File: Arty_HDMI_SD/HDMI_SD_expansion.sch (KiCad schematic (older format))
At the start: 54 parts, among them J2 1140084168, J4 2000-1-2-41-00-BK, J5 UE27AC54100, U1 TPS61232DRCT, U2 MAX3421EEHJ, Y1 KX-7_12,MHz

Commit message: Bug Fix
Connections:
- wire segments 238 -> 241
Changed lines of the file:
@@
+	1    0    0    -1
+$EndComp
+Wire Wire Line
+	6125 3600 6125 4125
+Wire Wire Line
+	5750 3600 5750 3750
+Wire Wire Line
+	6125 3600 5750 3600
+$Comp
+L power:GND #PWR?
+U 1 1 5D90A22E
+P 5750 3750
+F 0 "#PWR?" H 5750 3500 50  0001 C CNN
+F 1 "GND" H 5755 3577 50  0000 C CNN
+F 2 "" H 5750 3750 50  0001 C CNN
+F 3 "" H 5750 3750 50  0001 C CNN
+	1    5750 3750
 	1    0    0    -1
 $EndComp

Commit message: Added more testpads
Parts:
- added TP11, TP12, TP13, TP14, TP15: TP_SMD1MM, antmicro-footprints:Testpoint_smd_1mm, symbol antmicro_Test_Points:TP_SMD1MM
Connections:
- wire segments 241 -> 246
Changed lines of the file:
@@
 	6125 3600 5750 3600
 $Comp
-L power:GND #PWR?
+L power:GND #PWR01
 U 1 1 5D90A22E
 P 5750 3750
-F 0 "#PWR?" H 5750 3500 50  0001 C CNN
+F 0 "#PWR01" H 5750 3500 50  0001 C CNN
 F 1 "GND" H 5755 3577 50  0000 C CNN
 F 2 "" H 5750 3750 50  0001 C CNN
@@
 	1    0    0    -1
 $EndComp
+Wire Wire Line
+	9050 2100 8500 2100
+Wire Wire Line
+	9050 2200 8500 2200
+Wire Wire Line
+	9850 2300 10450 2300
+Wire Wire Line
+	9850 2400 10450 2400
+Wire Wire Line
+	9050 2400 8500 2400
+$Comp
+L antmicro_Test_Points:TP_SMD1MM TP11
+U 1 1 5D86FB45
+P 8400 2100
+F 0 "TP11" V 8400 2000 50  0000 C CNN
+F 1 "TP_SMD1MM" H 8400 2000 50  0001 C CNN
+F 2 "antmicro-footprints:Testpoint_smd_1mm" H 8600 2300 60  0001 L CNN
+F 3 "" H 8600 2400 60  0001 L CNN
+	1    8400 2100
+	0    1    1    0
+$EndComp
+$Comp
+L antmicro_Test_Points:TP_SMD1MM TP12
+U 1 1 5D86FCBB
+P 8400 2200
+F 0 "TP12" V 8400 2100 50  0000 C CNN
+F 1 "TP_SMD1MM" H 8400 2100 50  0001 C CNN
+F 2 "antmicro-footprints:Testpoint_smd_1mm" H 8600 2400 60  0001 L CNN
+F 3 "" H 8600 2500 60  0001 L CNN
+	1    8400 2200
+	0    1    1    0
+$EndComp
+$Comp
+L antmicro_Test_Points:TP_SMD1MM TP13
+U 1 1 5D86FD3B
+P 8400 2400
+F 0 "TP13" V 8400 2300 50  0000 C CNN
+F 1 "TP_SMD1MM" H 8400 2300 50  0001 C CNN
+F 2 "antmicro-footprints:Testpoint_smd_1mm" H 8600 2600 60  0001 L CNN
+F 3 "" H 8600 2700 60  0001 L CNN
+	1    8400 2400
+	0    1    1    0
+$EndComp
+$Comp
+L antmicro_Test_Points:TP_SMD1MM TP15
+U 1 1 5D86FDC5
+P 10550 2400
+F 0 "TP15" V 10550 2300 50  0000 C CNN
+F 1 "TP_SMD1MM" H 10550 2300 50  0001 C CNN
+F 2 "antmicro-footprints:Testpoint_smd_1mm" H 10750 2600 60  0001 L CNN
+F 3 "" H 10750 2700 60  0001 L CNN
+	1    10550 2400
+	0    -1   -1   0
+$EndComp
+$Comp
+L antmicro_Test_Points:TP_SMD1MM TP14
+U 1 1 5D86FF1F
+P 10550 2300
+F 0 "TP14" V 10550 2200 50  0000 C CNN
+F 1 "TP_SMD1MM" H 10550 2200 50  0001 C CNN
+F 2 "antmicro-footprints:Testpoint_smd_1mm" H 10750 2500 60  0001 L CNN
+F 3 "" H 10750 2600 60  0001 L CNN
+	1    10550 2300
+	0    -1   -1   0
+$EndComp
 $EndSCHEMATC

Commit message: Added TVS
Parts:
- removed C2, C3, C4, C5, C6, C7, C8, C9: C_100n_0402_6V3, antmicro-footprints:0402-cap, symbol HDMI_SD_expansion-rescue:C_100n_0402_6V3-antmicro_Capacitors_0402
- added IC1: TPD8S009DSMR, antmicro-footprints:R-PDSO-N15, symbol antmicroTVSDiodes:TPD8S009DSMR
- added R13, R14, R15, R16, R17, R18, R19, R20: R_0R_0402, antmicro-footprints:0402-res, symbol antmicroResistors0402:R_0R_0402
- C10, C12, C13, C14: symbol antmicro_Capacitors_0603:C_22u_0603 -> HDMI_SD_expansion-rescue:C_22u_0603-antmicro_Capacitors_0603
- C11: symbol antmicro_Capacitors_0402:C_10n_0402 -> HDMI_SD_expansion-rescue:C_10n_0402-antmicro_Capacitors_0402
- C16, C17: symbol antmicro_Capacitors_0402:C_22p_0402 -> HDMI_SD_expansion-rescue:C_22p_0402-antmicro_Capacitors_0402
- D1, D2: symbol antmicro_TVS_Diodes:PGB1010603MR -> HDMI_SD_expansion-rescue:PGB1010603MR-antmicro_TVS_Diodes
- J2: symbol antmicro_Memory_Connectors_PC_Card_Sockets:1140084168 -> HDMI_SD_expansion-rescue:1140084168-antmicro_Memory_Connectors_PC_Card_Sockets
- J4: symbol antmicro_USB_DVI_HDMI_Connectors:2000-1-2-41-00-BK -> HDMI_SD_expansion-rescue:2000-1-2-41-00-BK-antmicro_USB_DVI_HDMI_Connectors
- J5: symbol antmicro_USB_DVI_HDMI_Connectors:UE27AC54100 -> HDMI_SD_expansion-rescue:UE27AC54100-antmicro_USB_DVI_HDMI_Connectors
- JB1, JC1, JD1: symbol antmicro_Rectangular_Connectors_Headers_Male_Pins:0015912120 -> HDMI_SD_expansion-rescue:0015912120-antmicro_Rectangular_Connectors_Headers_Male_Pins
- L1: symbol antmicro_Fixed_Inductors:XFL4020-102MEB -> HDMI_SD_expansion-rescue:XFL4020-102MEB-antmicro_Fixed_Inductors
- N1: symbol antmicro_Mechanical_Parts:antmicro_logo -> HDMI_SD_expansion-rescue:antmicro_logo-antmicro_Mechanical_Parts
- R1, R2, R3, R4, R5, R6, R7: symbol antmicro_Resistors_0603:R_20k_0603 -> HDMI_SD_expansion-rescue:R_20k_0603-antmicro_Resistors_0603
- R10, R9: symbol antmicro_Resistors_0402:R_22R_0402 -> HDMI_SD_expansion-rescue:R_22R_0402-antmicro_Resistors_0402
- R11: symbol antmicro_Resistors_0603:R_10k_0603 -> HDMI_SD_expansion-rescue:R_10k_0603-antmicro_Resistors_0603
- R12: symbol antmicro_Resistors_0402:R_220R_0402 -> HDMI_SD_expansion-rescue:R_220R_0402-antmicro_Resistors_0402
- R8: symbol antmicro_Resistors_0603:R_0R_0603 -> HDMI_SD_expansion-rescue:R_0R_0603-antmicro_Resistors_0603
- TP1, TP10, TP11, TP12, TP13, TP14, TP15, TP2, TP3, TP4, TP5, TP6, TP7, TP8, TP9: symbol antmicro_Test_Points:TP_SMD1MM -> HDMI_SD_expansion-rescue:TP_SMD1MM-antmicro_Test_Points
- U1: symbol antmicro_DC_DC_Converters:TPS61232DRCT -> HDMI_SD_expansion-rescue:TPS61232DRCT-antmicro_DC_DC_Converters
- U2: symbol antmicro_Interface_Controllers:MAX3421EEHJ -> HDMI_SD_expansion-rescue:MAX3421EEHJ-antmicro_Interface_Controllers
- Y1: symbol antmicro_Oscillators:KX-7_12,MHz -> HDMI_SD_expansion-rescue:KX-7_12,MHz-antmicro_Oscillators
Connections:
- wire segments 246 -> 270
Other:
- note removed: "caps will be replaced with 0R by default"

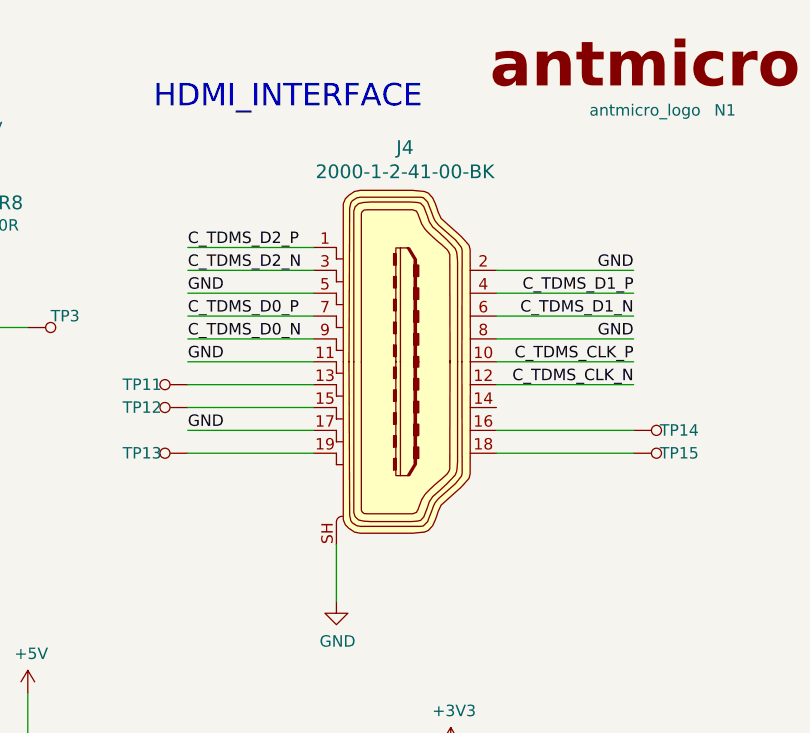
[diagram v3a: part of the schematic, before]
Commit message: Changed HDMI connector through hole
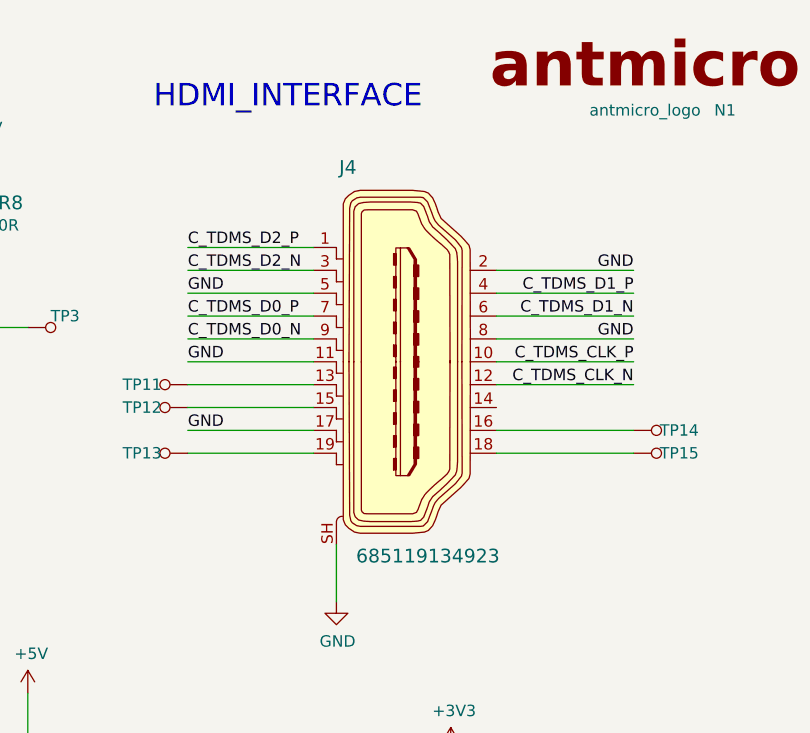
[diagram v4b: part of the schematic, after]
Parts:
- removed J4: 2000-1-2-41-00-BK, antmicro-footprints:HDMI_A_Female_2000-1-2-41-00-BK, symbol HDMI_SD_expansion-rescue:2000-1-2-41-00-BK-antmicro_USB_DVI_HDMI_Connectors
- added J4: 685119134923, antmicro-footprints:HDMI_A_Female_685119134923, symbol antmicroUSBDVIHDMIConnectors:685119134923
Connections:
- net C_TDMS_CLK_N: now also J4.12
- net C_TDMS_CLK_P: now also J4.10
- net C_TDMS_D0_N: now also J4.9
- net C_TDMS_D0_P: now also J4.7
- net C_TDMS_D1_N: now also J4.6
- net C_TDMS_D1_P: now also J4.4
- net C_TDMS_D2_N: now also J4.3
- net C_TDMS_D2_P: now also J4.1
- net GND: now also J4.11, J4.17, J4.2, J4.5, J4.8, J4.SH
- net at TP11.1: now also J4.13
- net at TP12.1: now also J4.15
- net at TP14.1: now also J4.16
- net at TP15.1: now also J4.18
- net at TP13.1: now also J4.19
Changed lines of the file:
@@
-	1    0    0    -1
-$EndComp
-$Comp
-L HDMI_SD_expansion-rescue:2000-1-2-41-00-BK-antmicro_USB_DVI_HDMI_Connectors J4
-U 1 1 5D6CFFFB
-P 9450 2000
-F 0 "J4" H 9450 2937 60  0000 C CNN
-F 1 "2000-1-2-41-00-BK" H 9450 2831 60  0000 C CNN
-F 2 "antmicro-footprints:HDMI_A_Female_2000-1-2-41-00-BK" H 9650 2200 60  0001 L CNN
-F 3 "http://www.cnctech.us/pdfs/2000-1-2-41-00-BK.pdf" H 9650 2300 60  0001 L CNN
-F 4 "2000-1-2-41-00-BK" H 9650 2500 60  0001 L CNN "MPN"
-F 5 "CNC Tech" H 9650 3100 60  0001 L CNN "Manufacturer"
-	1    9450 2000
 	1    0    0    -1
 $EndComp
@@
 Text Label 3450 4550 2    50   ~ 0
 GND
+$Comp
+L antmicroUSBDVIHDMIConnectors:685119134923 J4
+U 1 1 5DB26B59
+P 9450 2000
+F 0 "J4" H 9200 2850 60  0000 C CNN
+F 1 "685119134923" H 9550 1150 60  0000 C CNN
+F 2 "antmicro-footprints:HDMI_A_Female_685119134923" H 9650 2200 60  0001 L CNN
+F 3 "https://www.farnell.com/cad/1641702.pdf?_ga=2.75511573.1630328358.1571653391-156563690.1566371002&_gac=1.138144260.1570692453.EAIaIQobChMIsbyuq5WR5QIVhKiaCh1YMAxzEAYYBiABEgKWa_D_BwE" H 9650 2300 60  0001 L CNN
+F 4 "685119134923" H 9650 2500 60  0001 L CNN "MPN"
+F 5 "Amphenol" H 9650 3100 60  0001 L CNN "Manufacturer"
+	1    9450 2000
+	1    0    0    -1
+$EndComp
 $EndSCHEMATC
